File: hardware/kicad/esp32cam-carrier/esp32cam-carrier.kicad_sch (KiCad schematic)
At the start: 14 parts, among them Q1 2N7000

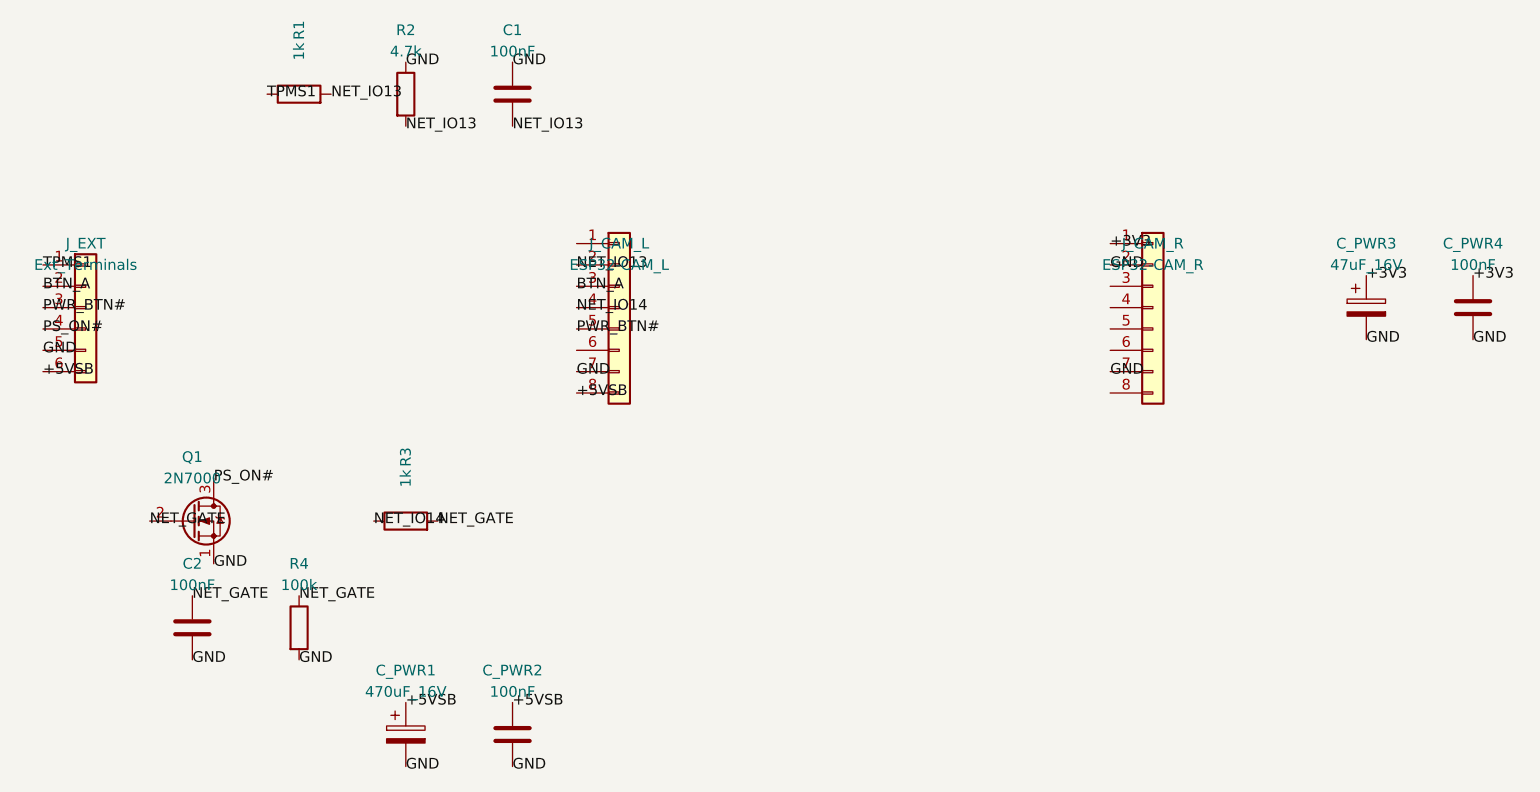
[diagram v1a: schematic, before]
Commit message: fix(hardware): align ESP32-CAM carrier PCB and docs to physical pinout
- Correct ESP32-CAM ASCII header diagrams in docs/pinout.md to match physical module
- Realign J_CAM_L and J_CAM_R socket mappings and isolate IO16 (PSRAM) in scripts/generate_carrier_pcb.py
- Re-route single-layer copper B.Cu with zero track crossings and 0 DRC violations
- Update J_EXT terminal ordering and coordinate maps in docs/esp32cam-carrier-pcb.md and docs/bom.md
- Sync hardware-targets spec and archive esp32cam-prototype-pcb and fix-esp32cam-carrier-pinout changes
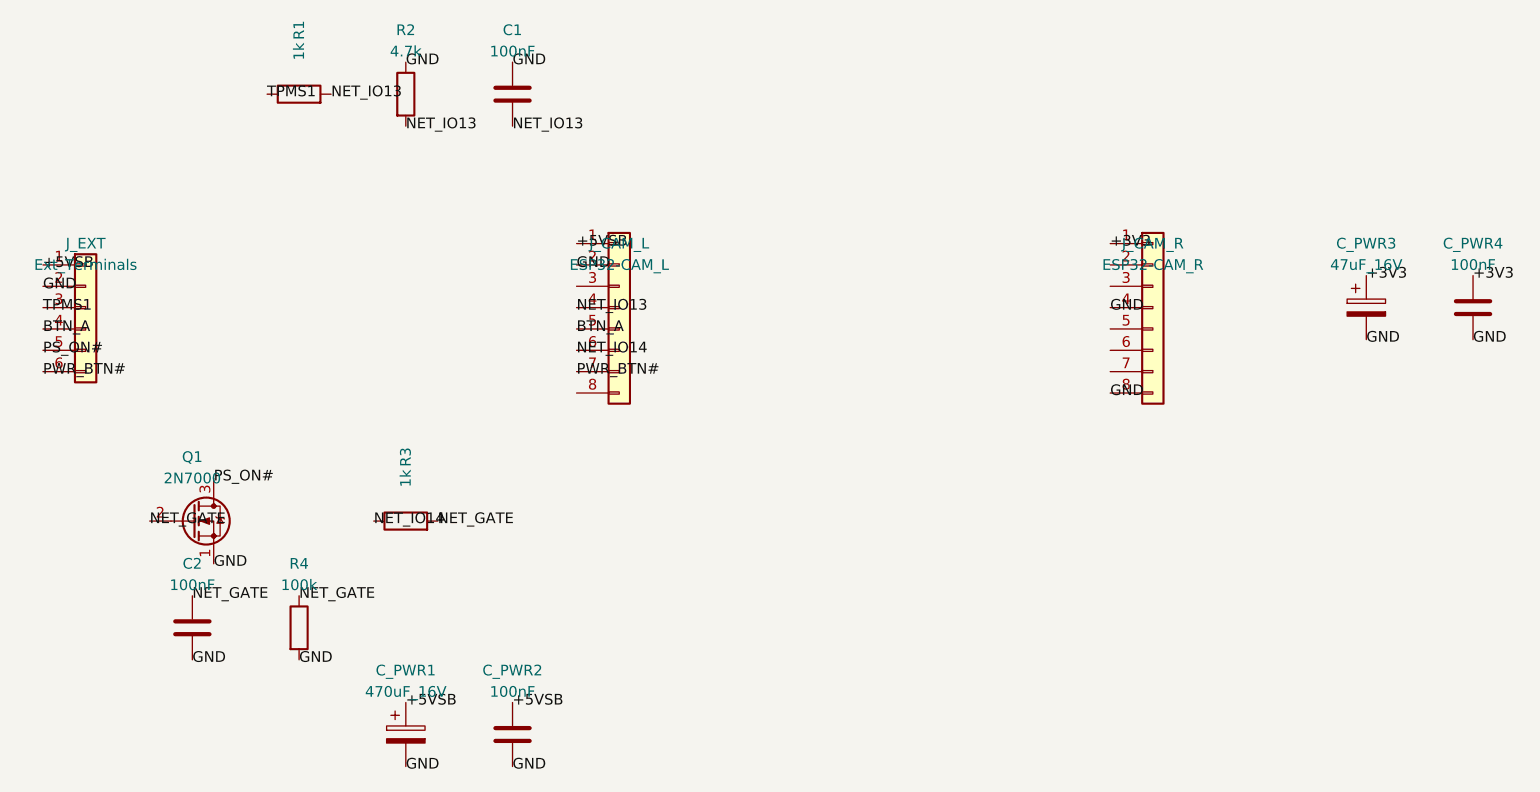
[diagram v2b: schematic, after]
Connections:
- net +5VSB: now also J_CAM_L.1 (Pin_1), J_EXT.1 (Pin_1); no longer J_CAM_L.8 (Pin_8), J_EXT.6 (Pin_6)
- net BTN_A: now also J_CAM_L.5 (Pin_5), J_EXT.4 (Pin_4); no longer J_CAM_L.3 (Pin_3), J_EXT.2 (Pin_2)
- net GND: now also J_CAM_L.2 (Pin_2), J_CAM_R.4 (Pin_4), J_CAM_R.8 (Pin_8), J_EXT.2 (Pin_2); no longer J_CAM_L.7 (Pin_7), J_CAM_R.2 (Pin_2), J_CAM_R.7 (Pin_7), J_EXT.5 (Pin_5)
- net NET_IO13: now also J_CAM_L.4 (Pin_4); no longer J_CAM_L.2 (Pin_2)
- net NET_IO14: now also J_CAM_L.6 (Pin_6); no longer J_CAM_L.4 (Pin_4)
- net PS_ON#: now also J_EXT.5 (Pin_5); no longer J_EXT.4 (Pin_4)
- net PWR_BTN#: now also J_CAM_L.7 (Pin_7), J_EXT.6 (Pin_6); no longer J_CAM_L.5 (Pin_5), J_EXT.3 (Pin_3)
- net TPMS1: now also J_EXT.3 (Pin_3); no longer J_EXT.1 (Pin_1)
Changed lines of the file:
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@@
 		(instances
 			(project "esp32cam-carrier"
-				(path "/386435ea-e18f-4c05-8ed0-30213534c88a"
+				(path "/b6757847-c15a-4907-8df8-aa7a3c4b041a"
 					(reference "J_EXT")
 					(unit 1)
@@
 		(instances
 			(project "esp32cam-carrier"
-				(path "/386435ea-e18f-4c05-8ed0-30213534c88a"
+				(path "/b6757847-c15a-4907-8df8-aa7a3c4b041a"
 					(reference "J_CAM_L")
 					(unit 1)
@@
 		(instances
 			(project "esp32cam-carrier"
-				(path "/386435ea-e18f-4c05-8ed0-30213534c88a"
+				(path "/b6757847-c15a-4907-8df8-aa7a3c4b041a"
 					(reference "J_CAM_R")
 					(unit 1)
@@
 		(instances
 			(project "esp32cam-carrier"
-				(path "/386435ea-e18f-4c05-8ed0-30213534c88a"
+				(path "/b6757847-c15a-4907-8df8-aa7a3c4b041a"
 					(reference "C_PWR1")
 					(unit 1)
@@
 		(instances
 			(project "esp32cam-carrier"
-				(path "/386435ea-e18f-4c05-8ed0-30213534c88a"
+				(path "/b6757847-c15a-4907-8df8-aa7a3c4b041a"
 					(reference "C_PWR2")
 					(unit 1)
@@
 		(instances
 			(project "esp32cam-carrier"
-				(path "/386435ea-e18f-4c05-8ed0-30213534c88a"
+				(path "/b6757847-c15a-4907-8df8-aa7a3c4b041a"
 					(reference "C_PWR3")
 					(unit 1)
@@
 		(instances
 			(project "esp32cam-carrier"
-				(path "/386435ea-e18f-4c05-8ed0-30213534c88a"
+				(path "/b6757847-c15a-4907-8df8-aa7a3c4b041a"
 					(reference "C_PWR4")
 					(unit 1)
@@
 		(instances
 			(project "esp32cam-carrier"
-				(path "/386435ea-e18f-4c05-8ed0-30213534c88a"
+				(path "/b6757847-c15a-4907-8df8-aa7a3c4b041a"
 					(reference "R1")
 					(unit 1)
@@
 		(instances
 			(project "esp32cam-carrier"
-				(path "/386435ea-e18f-4c05-8ed0-30213534c88a"
+				(path "/b6757847-c15a-4907-8df8-aa7a3c4b041a"
 					(reference "R2")
 					(unit 1)
@@
 		(instances
 			(project "esp32cam-carrier"
-				(path "/386435ea-e18f-4c05-8ed0-30213534c88a"
+				(path "/b6757847-c15a-4907-8df8-aa7a3c4b041a"
 					(reference "C1")
 					(unit 1)
@@
 		(instances
 			(project "esp32cam-carrier"
-				(path "/386435ea-e18f-4c05-8ed0-30213534c88a"
+				(path "/b6757847-c15a-4907-8df8-aa7a3c4b041a"
 					(reference "Q1")
 					(unit 1)
@@
 		(instances
 			(project "esp32cam-carrier"
-				(path "/386435ea-e18f-4c05-8ed0-30213534c88a"
+				(path "/b6757847-c15a-4907-8df8-aa7a3c4b041a"
 					(reference "R3")
 					(unit 1)
@@
 		(instances
 			(project "esp32cam-carrier"
-				(path "/386435ea-e18f-4c05-8ed0-30213534c88a"
+				(path "/b6757847-c15a-4907-8df8-aa7a3c4b041a"
 					(reference "R4")
 					(unit 1)
@@
 		(instances
 			(project "esp32cam-carrier"
-				(path "/386435ea-e18f-4c05-8ed0-30213534c88a"
+				(path "/b6757847-c15a-4907-8df8-aa7a3c4b041a"
 					(reference "C2")
 					(unit 1)
@@
 		)
 	)
-	(label "TPMS1" (at 45.72 58.42 0) (effects (font (size 1.27 1.27))))
-	(label "BTN_A" (at 45.72 60.96 0) (effects (font (size 1.27 1.27))))
-	(label "PWR_BTN#" (at 45.72 63.5 0) (effects (font (size 1.27 1.27))))
-	(label "PS_ON#" (at 45.72 66.04 0) (effects (font (size 1.27 1.27))))
-	(label "GND" (at 45.72 68.58 0) (effects (font (size 1.27 1.27))))
-	(label "+5VSB" (at 45.72 71.12 0) (effects (font (size 1.27 1.27))))
-	(label "NET_IO13" (at 109.22 58.42 0) (effects (font (size 1.27 1.27))))
-	(label "BTN_A" (at 109.22 60.96 0) (effects (font (size 1.27 1.27))))
-	(label "NET_IO14" (at 109.22 63.5 0) (effects (font (size 1.27 1.27))))
-	(label "PWR_BTN#" (at 109.22 66.04 0) (effects (font (size 1.27 1.27))))
-	(label "GND" (at 109.22 71.12 0) (effects (font (size 1.27 1.27))))
-	(label "+5VSB" (at 109.22 73.66 0) (effects (font (size 1.27 1.27))))
+	(label "+5VSB" (at 45.72 58.42 0) (effects (font (size 1.27 1.27))))
+	(label "GND" (at 45.72 60.96 0) (effects (font (size 1.27 1.27))))
+	(label "TPMS1" (at 45.72 63.5 0) (effects (font (size 1.27 1.27))))
+	(label "BTN_A" (at 45.72 66.04 0) (effects (font (size 1.27 1.27))))
+	(label "PS_ON#" (at 45.72 68.58 0) (effects (font (size 1.27 1.27))))
+	(label "PWR_BTN#" (at 45.72 71.12 0) (effects (font (size 1.27 1.27))))
+	(label "+5VSB" (at 109.22 55.88 0) (effects (font (size 1.27 1.27))))
+	(label "GND" (at 109.22 58.42 0) (effects (font (size 1.27 1.27))))
+	(label "NET_IO13" (at 109.22 63.5 0) (effects (font (size 1.27 1.27))))
+	(label "BTN_A" (at 109.22 66.04 0) (effects (font (size 1.27 1.27))))
+	(label "NET_IO14" (at 109.22 68.58 0) (effects (font (size 1.27 1.27))))
+	(label "PWR_BTN#" (at 109.22 71.12 0) (effects (font (size 1.27 1.27))))
 	(label "+3V3" (at 172.72 55.88 0) (effects (font (size 1.27 1.27))))
-	(label "GND" (at 172.72 58.42 0) (effects (font (size 1.27 1.27))))
-	(label "GND" (at 172.72 71.12 0) (effects (font (size 1.27 1.27))))
+	(label "GND" (at 172.72 63.5 0) (effects (font (size 1.27 1.27))))
+	(label "GND" (at 172.72 73.66 0) (effects (font (size 1.27 1.27))))
 	(label "+5VSB" (at 88.9 110.49 0) (effects (font (size 1.27 1.27))))
 	(label "GND" (at 88.9 118.11 0) (effects (font (size 1.27 1.27))))
@@
 	(label "GND" (at 63.5 105.41 0) (effects (font (size 1.27 1.27))))
 	(sheet_instances
-		(path "/386435ea-e18f-4c05-8ed0-30213534c88a"
+		(path "/b6757847-c15a-4907-8df8-aa7a3c4b041a"
 			(page "1")
 		)

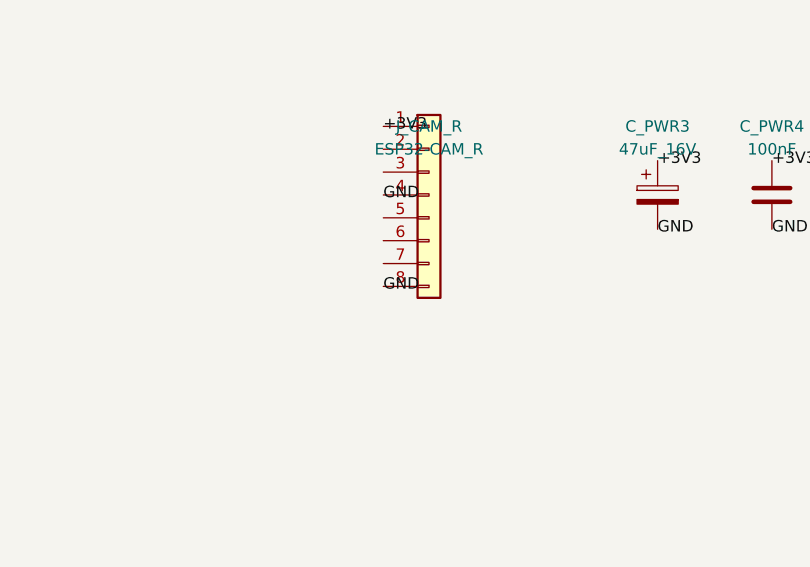
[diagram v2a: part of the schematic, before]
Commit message: fix(hardware): isolate ESP32-CAM GND/R reset pin on carrier PCB
Disconnect J_CAM_R pin 8 (GND/R) from ground to prevent holding the ESP32-CAM in hardware reset on clone boards, reroute the bottom ground bus via the left edge, and update documentation and specs.
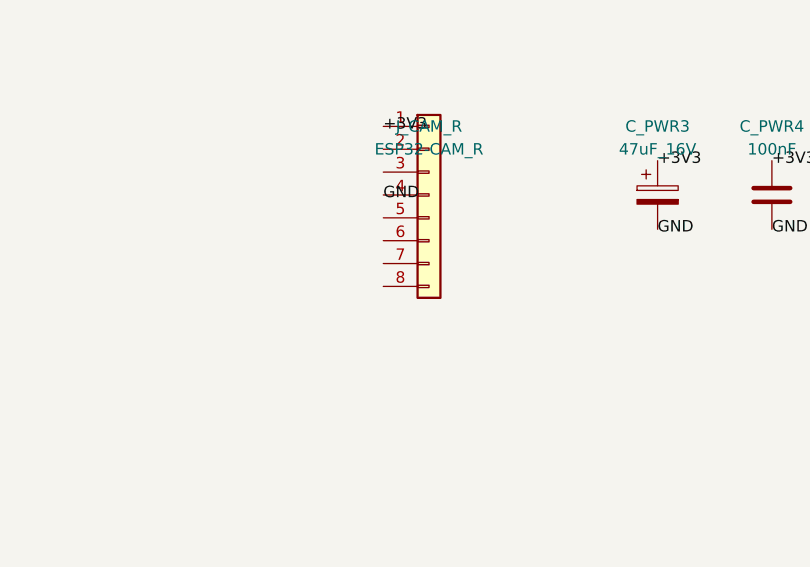
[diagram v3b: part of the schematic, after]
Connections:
- net GND: no longer J_CAM_R.8 (Pin_8)
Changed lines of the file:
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@@
 		(instances
 			(project "esp32cam-carrier"
-				(path "/b6757847-c15a-4907-8df8-aa7a3c4b041a"
+				(path "/f9fb3ae6-6c6b-44c8-a4d8-f85f21614183"
 					(reference "J_EXT")
 					(unit 1)
@@
 		(instances
 			(project "esp32cam-carrier"
-				(path "/b6757847-c15a-4907-8df8-aa7a3c4b041a"
+				(path "/f9fb3ae6-6c6b-44c8-a4d8-f85f21614183"
 					(reference "J_CAM_L")
 					(unit 1)
@@
 		(instances
 			(project "esp32cam-carrier"
-				(path "/b6757847-c15a-4907-8df8-aa7a3c4b041a"
+				(path "/f9fb3ae6-6c6b-44c8-a4d8-f85f21614183"
 					(reference "J_CAM_R")
 					(unit 1)
@@
 		(instances
 			(project "esp32cam-carrier"
-				(path "/b6757847-c15a-4907-8df8-aa7a3c4b041a"
+				(path "/f9fb3ae6-6c6b-44c8-a4d8-f85f21614183"
 					(reference "C_PWR1")
 					(unit 1)
@@
 		(instances
 			(project "esp32cam-carrier"
-				(path "/b6757847-c15a-4907-8df8-aa7a3c4b041a"
+				(path "/f9fb3ae6-6c6b-44c8-a4d8-f85f21614183"
 					(reference "C_PWR2")
 					(unit 1)
@@
 		(instances
 			(project "esp32cam-carrier"
-				(path "/b6757847-c15a-4907-8df8-aa7a3c4b041a"
+				(path "/f9fb3ae6-6c6b-44c8-a4d8-f85f21614183"
 					(reference "C_PWR3")
 					(unit 1)
@@
 		(instances
 			(project "esp32cam-carrier"
-				(path "/b6757847-c15a-4907-8df8-aa7a3c4b041a"
+				(path "/f9fb3ae6-6c6b-44c8-a4d8-f85f21614183"
 					(reference "C_PWR4")
 					(unit 1)
@@
 		(instances
 			(project "esp32cam-carrier"
-				(path "/b6757847-c15a-4907-8df8-aa7a3c4b041a"
+				(path "/f9fb3ae6-6c6b-44c8-a4d8-f85f21614183"
 					(reference "R1")
 					(unit 1)
@@
 		(instances
 			(project "esp32cam-carrier"
-				(path "/b6757847-c15a-4907-8df8-aa7a3c4b041a"
+				(path "/f9fb3ae6-6c6b-44c8-a4d8-f85f21614183"
 					(reference "R2")
 					(unit 1)
@@
 		(instances
 			(project "esp32cam-carrier"
-				(path "/b6757847-c15a-4907-8df8-aa7a3c4b041a"
+				(path "/f9fb3ae6-6c6b-44c8-a4d8-f85f21614183"
 					(reference "C1")
 					(unit 1)
@@
 		(instances
 			(project "esp32cam-carrier"
-				(path "/b6757847-c15a-4907-8df8-aa7a3c4b041a"
+				(path "/f9fb3ae6-6c6b-44c8-a4d8-f85f21614183"
 					(reference "Q1")
 					(unit 1)
@@
 		(instances
 			(project "esp32cam-carrier"
-				(path "/b6757847-c15a-4907-8df8-aa7a3c4b041a"
+				(path "/f9fb3ae6-6c6b-44c8-a4d8-f85f21614183"
 					(reference "R3")
 					(unit 1)
@@
 		(instances
 			(project "esp32cam-carrier"
-				(path "/b6757847-c15a-4907-8df8-aa7a3c4b041a"
+				(path "/f9fb3ae6-6c6b-44c8-a4d8-f85f21614183"
 					(reference "R4")
 					(unit 1)
@@
 		(instances
 			(project "esp32cam-carrier"
-				(path "/b6757847-c15a-4907-8df8-aa7a3c4b041a"
+				(path "/f9fb3ae6-6c6b-44c8-a4d8-f85f21614183"
 					(reference "C2")
 					(unit 1)
@@
 	(label "+3V3" (at 172.72 55.88 0) (effects (font (size 1.27 1.27))))
 	(label "GND" (at 172.72 63.5 0) (effects (font (size 1.27 1.27))))
-	(label "GND" (at 172.72 73.66 0) (effects (font (size 1.27 1.27))))
 	(label "+5VSB" (at 88.9 110.49 0) (effects (font (size 1.27 1.27))))
 	(label "GND" (at 88.9 118.11 0) (effects (font (size 1.27 1.27))))
@@
 	(label "GND" (at 63.5 105.41 0) (effects (font (size 1.27 1.27))))
 	(sheet_instances
-		(path "/b6757847-c15a-4907-8df8-aa7a3c4b041a"
+		(path "/f9fb3ae6-6c6b-44c8-a4d8-f85f21614183"
 			(page "1")
 		)
